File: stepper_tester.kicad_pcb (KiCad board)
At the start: 2 copper layers, 57.7 x 58.2 mm, 9 parts, among them J1 Conn_01x08, J2 Conn_01x08, J3 Conn_01x04, U1 BluePill_STM32F103C

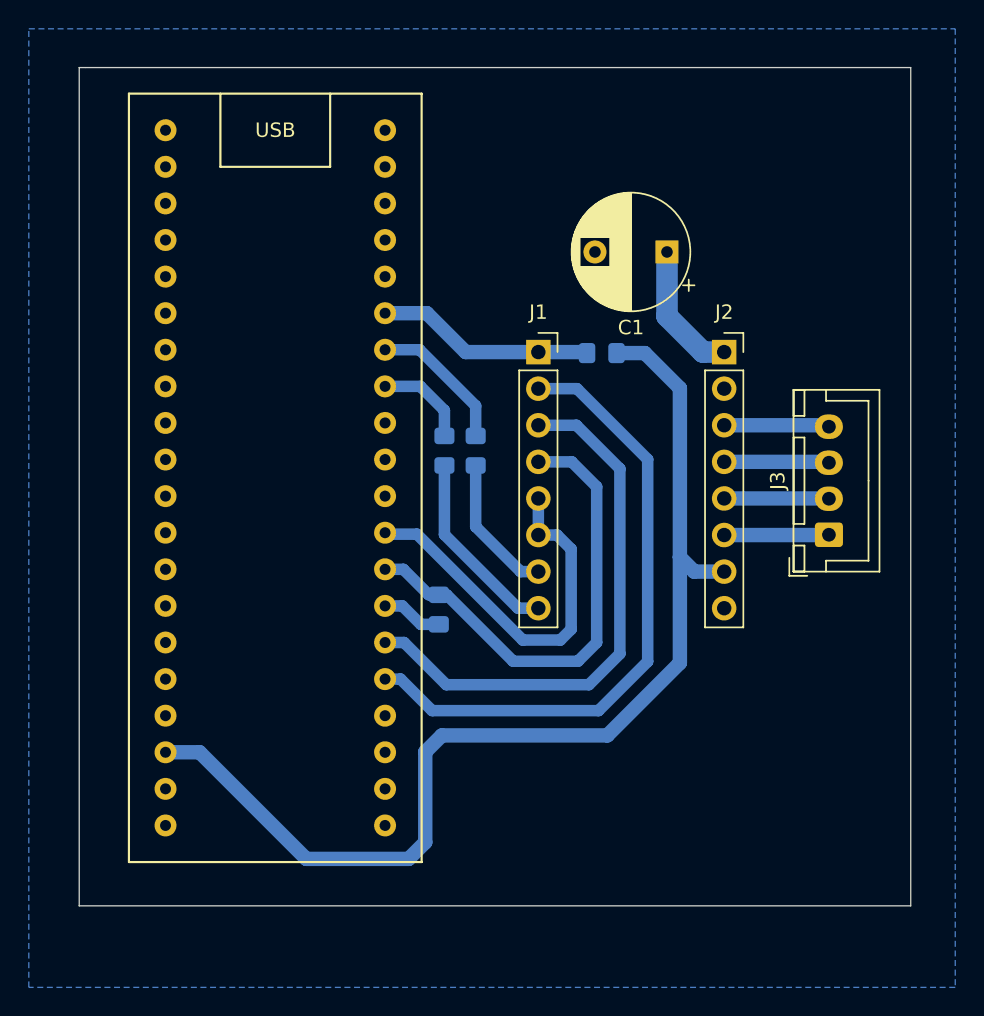
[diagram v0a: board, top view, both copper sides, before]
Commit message: Power connector, 90 deg rotation
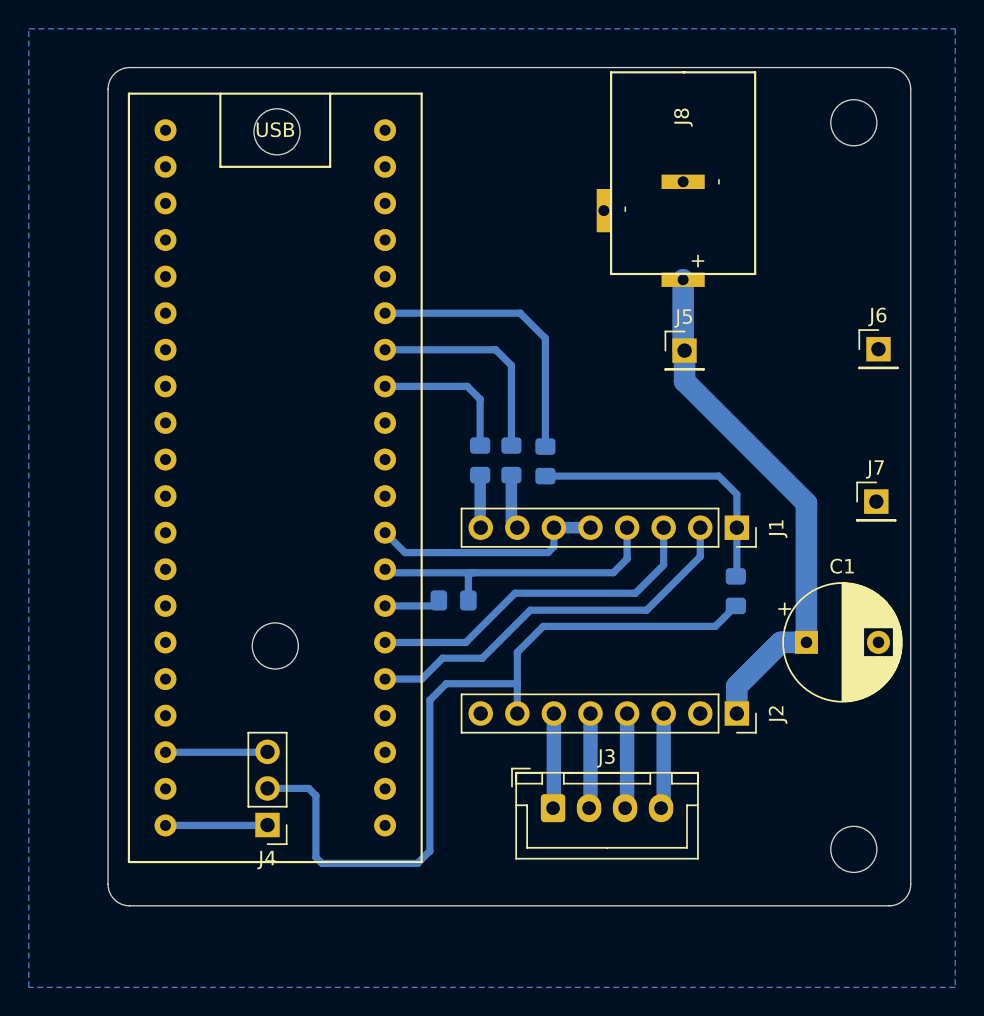
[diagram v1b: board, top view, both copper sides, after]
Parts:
- added H1: MountingHole, MountingHole:MountingHole_3.2mm_M3, F.Cu at (94.3, 97.1)
- added H2: MountingHole, MountingHole:MountingHole_3.2mm_M3, F.Cu at (94.3, 46.7)
- added H3: MountingHole, MountingHole:MountingHole_3.2mm_M3, F.Cu at (54.2, 83.0)
- added H4: MountingHole, MountingHole:MountingHole_3.2mm_M3, F.Cu at (54.3, 47.3)
- added J4: Conn_01x03, Connector_PinHeader_2.54mm:PinHeader_1x03_P2.54mm_Vertical, F.Cu at (53.6, 95.4)
- added J5: Conn_01x01, Connector_PinHeader_2.54mm:PinHeader_1x01_P2.54mm_Vertical, F.Cu at (82.6, 62.5)
- added J6: Conn_01x01, Connector_PinHeader_2.54mm:PinHeader_1x01_P2.54mm_Vertical, F.Cu at (96.1, 62.4)
- added J7: Conn_01x01, Connector_PinHeader_2.54mm:PinHeader_1x01_P2.54mm_Vertical, F.Cu at (95.9, 73.0)
- added J8: Conn_01x03, posad:Socket5.5x2.1, F.Cu at (82.5, 43.2)
- added R5: 100, Resistor_SMD:R_0805_2012Metric_Pad1.15x1.40mm_HandSolder, B.Cu at (72.9, 70.2)
- moved C1 28.8 mm to (91.1, 82.7), turned to 0 degrees
- moved J3 27.0 mm to (73.5, 94.2), turned to 0 degrees
- moved J2 25.1 mm to (86.2, 87.7), turned to 270 degrees
- moved R2 19.0 mm to (86.2, 79.2), turned to 90 degrees
- moved J1 18.4 mm to (86.2, 74.8), turned to 270 degrees
- moved R1 2.57 mm to (70.6, 70.1)
- moved R3 2.57 mm to (68.4, 70.1)
- moved R4 1.21 mm to (66.6, 79.8), turned to 0 degrees
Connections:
- J1 pad 1: EN -> Net-(J1-Pad1)
- J2 pad 7: VDD_5V -> VDD_DRV
- R2 pad 1: VDD_5V -> VDD_DRV
- R2 pad 2: EN -> Net-(J1-Pad1)
- U1 pad 40: (no net) -> VDD_3V3
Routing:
- net VDD_5V: track 76.1 -> 7.09 mm
- net VDD_DRV: track 0.00 -> 54.1 mm
- net VM_VDD: track 9.46 -> 40.7 mm
- net Net-(J1-Pad1): track 0.00 -> 19.5 mm
- net MS1: track 44.2 -> 27.4 mm
- net MS2: track 38.2 -> 24.2 mm
- net MS3: track 33.4 -> 21.5 mm
- net SLEEP: track 27.1 -> 16.3 mm
- net Net-(J1-Pad8): track 13.4 -> 3.67 mm
- net VDD_3V3: track 0.00 -> 7.09 mm
- net Net-(J1-Pad7): track 9.89 -> 3.82 mm
- net STEP: track 9.99 -> 14.8 mm
- net EN: track 15.2 -> 19.4 mm
- net DIR: track 6.58 -> 10.2 mm
- net 1B: track 7.28 -> 6.59 mm
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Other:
- board size 57.7 x 58.2 mm -> 55.7 x 58.2 mm

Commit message: Схема
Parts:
- J8: footprint posad:Socket5.5x2.1 -> power:DC55x21THT
- moved J8 4.59 mm to (77.9, 43.0)
- moved J6 3.49 mm to (95.5, 58.9)
- moved J7 2.95 mm to (95.5, 70.0)
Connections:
- J8 pad 1: (no net) -> VM_VDD
- J8 pad 2: VM_VDD -> GND
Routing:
- net VM_VDD: track 40.7 -> 41.8 mm
